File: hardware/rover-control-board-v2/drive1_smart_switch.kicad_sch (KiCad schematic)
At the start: 23 parts

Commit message: progress
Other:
- moved on the sheet: C2, C3
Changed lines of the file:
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@@
 	)
 	(junction
-		(at 193.04 149.86)
+		(at 198.12 149.86)
 		(diameter 0)
 		(color 0 0 0 0)
@@
 	)
 	(junction
-		(at 193.04 129.54)
-		(diameter 0)
-		(color 0 0 0 0)
-	)
-	(junction
 		(at 177.8 121.92)
 		(diameter 0)
@@
 	)
 	(junction
-		(at 204.47 129.54)
+		(at 60.96 29.21)
 		(diameter 0)
 		(color 0 0 0 0)
 	)
 	(junction
-		(at 60.96 29.21)
+		(at 204.47 129.54)
 		(diameter 0)
 		(color 0 0 0 0)
@@
 	)
 	(junction
+		(at 198.12 129.54)
+		(diameter 0)
+		(color 0 0 0 0)
+	)
+	(junction
 		(at 215.9 121.92)
 		(diameter 0)
@@
 	(wire
 		(pts
-			(xy 204.47 135.89) (xy 204.47 129.54)
+			(xy 209.55 135.89) (xy 209.55 134.62)
 		)
 		(stroke
@@
 	(wire
 		(pts
-			(xy 193.04 143.51) (xy 193.04 149.86)
+			(xy 198.12 143.51) (xy 198.12 149.86)
 		)
 		(stroke
@@
 	(wire
 		(pts
-			(xy 193.04 135.89) (xy 193.04 129.54)
+			(xy 198.12 135.89) (xy 198.12 129.54)
 		)
 		(stroke
@@
 	(wire
 		(pts
-			(xy 193.04 149.86) (xy 204.47 149.86)
+			(xy 198.12 149.86) (xy 209.55 149.86)
 		)
 		(stroke
@@
 	(wire
 		(pts
-			(xy 204.47 149.86) (xy 204.47 143.51)
+			(xy 209.55 149.86) (xy 209.55 143.51)
 		)
 		(stroke
@@
 	(wire
 		(pts
-			(xy 193.04 129.54) (xy 204.47 129.54)
+			(xy 193.04 129.54) (xy 198.12 129.54)
 		)
 		(stroke
@@
 	(wire
 		(pts
-			(xy 193.04 151.13) (xy 193.04 149.86)
+			(xy 198.12 151.13) (xy 198.12 149.86)
+		)
+		(stroke
+			(width 0)
+			(type default)
+		)
+	)
+	(wire
+		(pts
+			(xy 204.47 129.54) (xy 204.47 134.62)
 		)
 		(stroke
@@
 	(wire
 		(pts
+			(xy 198.12 129.54) (xy 204.47 129.54)
+		)
+		(stroke
+			(width 0)
+			(type default)
+		)
+	)
+	(wire
+		(pts
 			(xy 63.5 30.48) (xy 63.5 29.21)
 		)
@@
 		(pts
 			(xy 31.75 57.15) (xy 31.75 58.42)
+		)
+		(stroke
+			(width 0)
+			(type default)
+		)
+	)
+	(wire
+		(pts
+			(xy 209.55 134.62) (xy 204.47 134.62)
 		)
 		(stroke
@@
 	(hierarchical_label "PWR_IN"
 		(shape input)
-		(at 204.47 129.54 0)
+		(at 204.47 132.08 0)
 		(effects
 			(font
@@
 	(symbol
 		(lib_id "power:GND")
-		(at 193.04 151.13 0)
+		(at 198.12 151.13 0)
 		(unit 1)
 		(body_style 1)
@@
 		(fields_autoplaced yes)
 		(property "Reference" "#PWR08"
-			(at 193.04 157.48 0)
+			(at 198.12 157.48 0)
 			(hide yes)
 			(show_name no)
@@
 		)
 		(property "Value" "GND"
-			(at 193.04 156.21 0)
+			(at 198.12 156.21 0)
 			(show_name no)
 			(do_not_autoplace no)
@@
 		)
 		(property "Footprint" ""
-			(at 193.04 151.13 0)
+			(at 198.12 151.13 0)
 			(hide yes)
 			(show_name no)
@@
 		)
 		(property "Datasheet" ""
-			(at 193.04 151.13 0)
+			(at 198.12 151.13 0)
 			(hide yes)
 			(show_name no)
@@
 		)
 		(property "Description" "Power symbol creates a global label with name \"GND\" , ground"
-			(at 193.04 151.13 0)
+			(at 198.12 151.13 0)
 			(hide yes)
 			(show_name no)
@@
 	(symbol
 		(lib_id "Device:C")
-		(at 193.04 139.7 0)
+		(at 198.12 139.7 0)
 		(unit 1)
 		(body_style 1)
@@
 		(dnp no)
 		(property "Reference" "C2"
-			(at 195.58 138.43 0)
+			(at 200.66 138.43 0)
 			(show_name no)
 			(do_not_autoplace no)
@@
 		)
 		(property "Value" "10nF"
-			(at 195.58 140.97 0)
+			(at 200.66 140.97 0)
 			(show_name no)
 			(do_not_autoplace no)
@@
 		)
 		(property "Footprint" ""
-			(at 194.0052 143.51 0)
+			(at 199.0852 143.51 0)
 			(hide yes)
 			(show_name no)
@@
 		)
 		(property "Datasheet" ""
-			(at 193.04 139.7 0)
+			(at 198.12 139.7 0)
 			(hide yes)
 			(show_name no)
@@
 		)
 		(property "Description" "Unpolarized capacitor"
-			(at 193.04 139.7 0)
+			(at 198.12 139.7 0)
 			(hide yes)
 			(show_name no)
@@
 	(symbol
 		(lib_id "Device:C")
-		(at 204.47 139.7 0)
+		(at 209.55 139.7 0)
 		(unit 1)
 		(body_style 1)
@@
 		(dnp no)
 		(property "Reference" "C3"
-			(at 207.01 138.43 0)
+			(at 212.09 138.43 0)
 			(show_name no)
 			(do_not_autoplace no)
@@
 		)
 		(property "Value" "100nF"
-			(at 207.01 140.97 0)
+			(at 212.09 140.97 0)
 			(show_name no)
 			(do_not_autoplace no)
@@
 		)
 		(property "Footprint" ""
-			(at 205.4352 143.51 0)
+			(at 210.5152 143.51 0)
 			(hide yes)
 			(show_name no)
@@
 		)
 		(property "Datasheet" ""
-			(at 204.47 139.7 0)
+			(at 209.55 139.7 0)
 			(hide yes)
 			(show_name no)
@@
 		)
 		(property "Description" "Unpolarized capacitor"
-			(at 204.47 139.7 0)
-			(hide yes)
-			(show_name no)
+			(at 209.55 139.7 0)
+			(hide yes)
+			(show_name no)

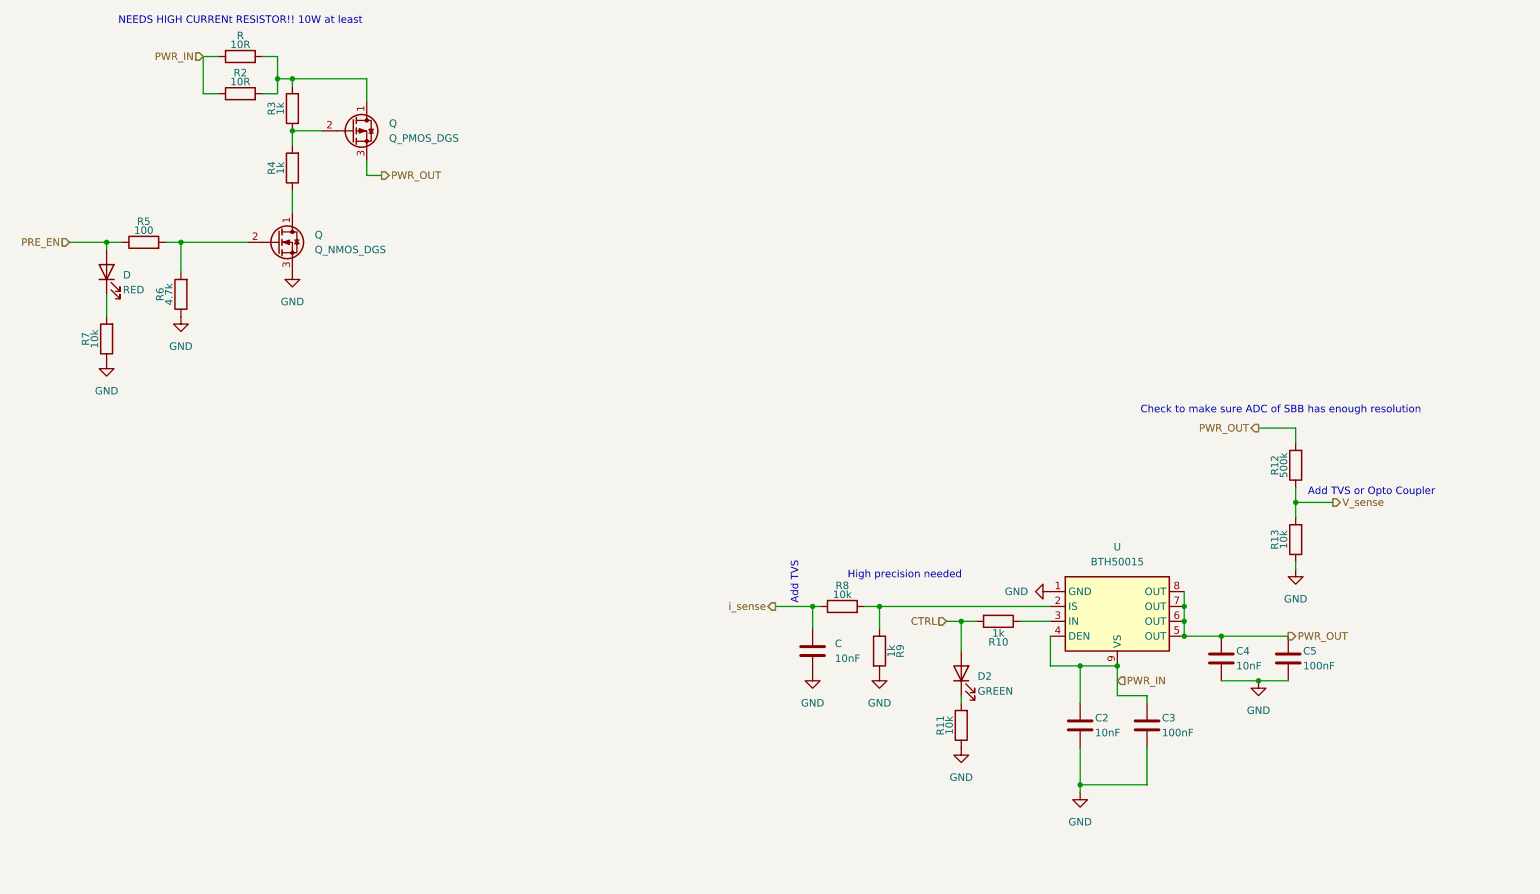
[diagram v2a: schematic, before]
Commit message: Channels routed, temp bus pending
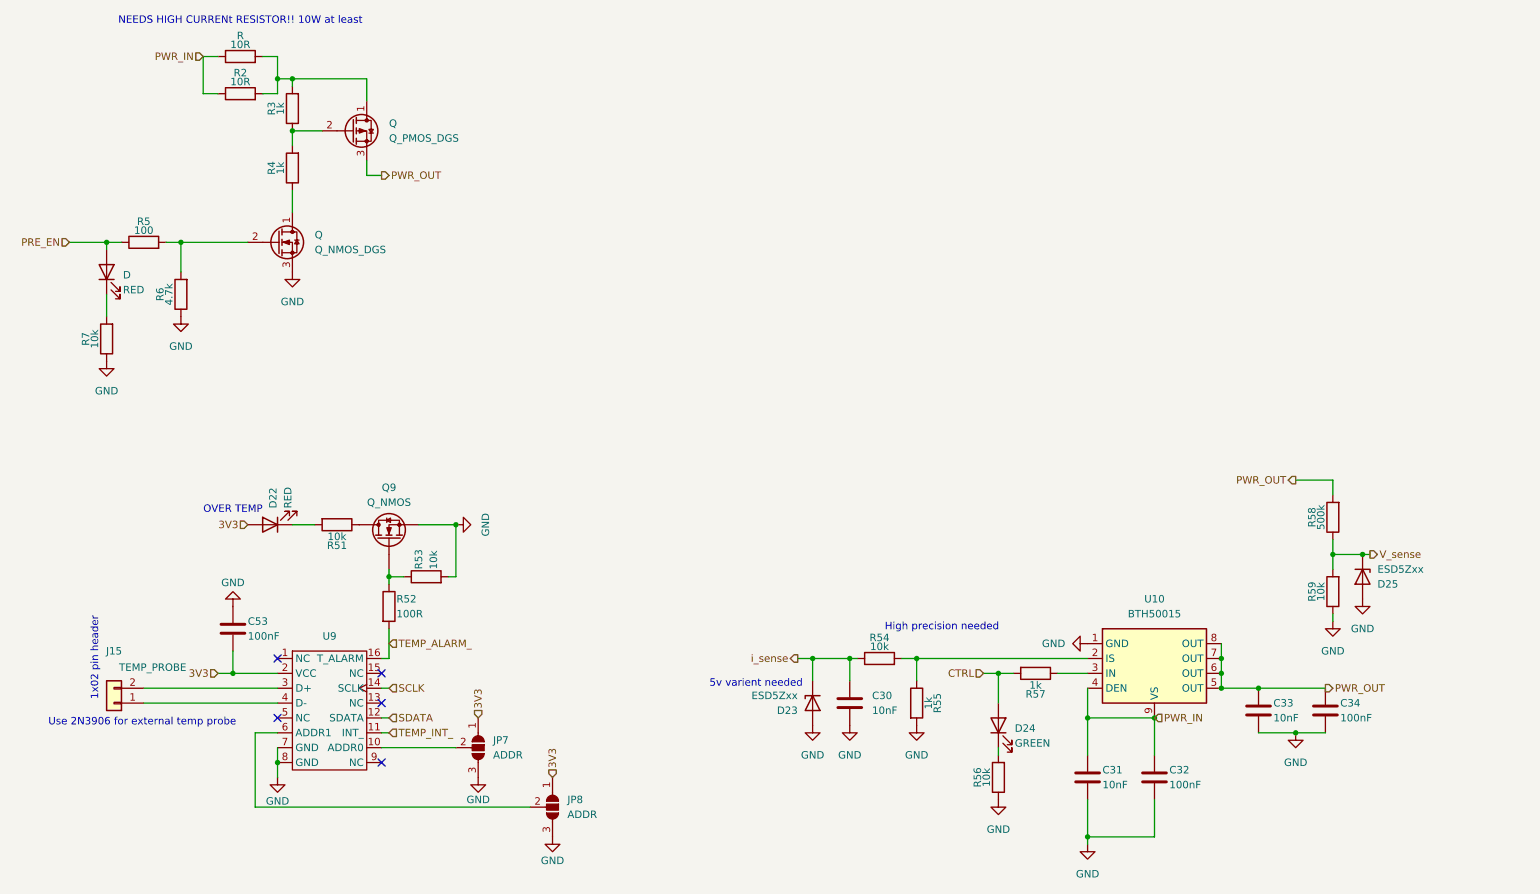
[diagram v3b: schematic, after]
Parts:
- removed C, C2, C4: 10nF, symbol Device:C
- removed C3, C5: 100nF, symbol Device:C
- removed D2: GREEN, symbol Device:LED
- removed R10, R9: 1k, symbol Device:R
- removed R11, R13, R8: 10k, symbol Device:R
- removed R12: 500k, symbol Device:R
- removed U: BTH50015, Package_SO:Infineon_PG-TSDSO-14-22, symbol component_library:BTH50015
- added C30, C31, C33: 10nF, symbol Device:C
- added C32, C34, C53: 100nF, symbol Device:C
- added D22: RED, symbol Device:LED
- added D23, D25: ESD5Zxx, Diode_SMD:D_SOD-523, symbol Diode:ESD5Zxx
- added D24: GREEN, symbol Device:LED
- added J15: TEMP_PROBE, symbol Connector_Generic:Conn_01x02
- added JP7, JP8: ADDR, Jumper:SolderJumper-3_P1.3mm_Open_Pad1.0x1.5mm, symbol Jumper:SolderJumper_3_Open
- added Q9: Q_NMOS, symbol Device:Q_NMOS
- added R51, R53, R54, R56, R59: 10k, symbol Device:R
- added R52: 100R, symbol Device:R
- added R55, R57: 1k, symbol Device:R
- added R58: 500k, symbol Device:R
- added U10: BTH50015, Package_SO:Infineon_PG-TSDSO-14-22, symbol component_library:BTH50015
- added U9: (no value), footprints:LM82, symbol component_library:LM82
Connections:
- net CTRL: now also D24.2 (A), R57.2
- net GND: now also C30.2, C31.2, C32.2, C33.2, C34.2, C53.1, D23.2 (A), D25.2 (A), JP7.3 (B), JP8.3 (B), Q9.S, R53.2, R55.2, R56.1, R59.1, U10.1 (GND), U9.7 (GND), U9.8 (GND)
- net PWR_IN: now also C31.1, C32.1, U10.4 (DEN), U10.9 (VS)
- net PWR_OUT: now also C33.1, C34.1, R58.2, U10.5 (OUT), U10.6 (OUT), U10.7 (OUT), U10.8 (OUT)
- net V_sense: now also D25.1 (K), R58.1, R59.2
- net i_sense: now also C30.1, D23.1 (K), R54.1
- new net: JP8.2 (C), U9.6 (ADDR1)
- new net: R54.2, R55.1, U10.2 (IS)
- new net: Q9.G, R52.1, R53.1
- new net: D24.1 (K), R56.2
- new net: Q9.D, R51.1
- new net: D22.1 (K), R51.2
- new net: R57.1, U10.3 (IN)
- new net: JP7.2 (C), U9.10 (ADDR0)
- new net: J15.2 (Pin_2), U9.3 (D+)
- new net: J15.1 (Pin_1), U9.4 (D-)
- new net 3V3: C53.2, D22.2 (A), JP7.1 (A), JP8.1 (A), U9.2 (VCC)
- new net SCLK: U9.14 (SCLK)
- new net SDATA: U9.12 (SDATA)
- new net TEMP_ALARM_: R52.2, U9.16 (T_ALARM)
- new net TEMP_INT_: U9.11 (INT_)
- no-connect marks 0 -> 5
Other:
- note added: "1x02 pin header"
- note added: "5v varient needed"
- note added: "OVER TEMP"
- note added: "Use 2N3906 for external temp probe"
- note removed: "Add TVS"
- note removed: "Add TVS or Opto Coupler"
- note removed: "Check to make sure ADC of SBB has enough resolution"

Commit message: Bus routed
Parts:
- renumbered C53 to C34, C30 to C35, C31 to C36, C32 to C37, C33 to C38, C34 to C39, D to D20, D22 to D21, D23 to D22, D24 to D23, D25 to D24, J15 to J13, Q to Q12, Q to Q13, Q9 to Q14, R7 to R62, R5 to R63, R6 to R64, R to R65, R2 to R66, R3 to R67, R4 to R68, R51 to R69, R52 to R70, R53 to R71, R54 to R72, R55 to R73, R56 to R74, R57 to R75, R58 to R76, R59 to R77, U9 to U11, U10 to U12

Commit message: revamping channel switches
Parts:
- renumbered C34 to C28, C35 to C29, C36 to C30, C37 to C31, C38 to C32, C39 to C33, J13 to J14, R62 to R61, R63 to R62, R64 to R63, R65 to R64, R66 to R65, R67 to R66, R68 to R67, R69 to R68, R70 to R69, R71 to R70, R72 to R71, R73 to R72, R74 to R73, R75 to R74, R76 to R75, R77 to R76, U11 to U10, U12 to U11

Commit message: Minor fixes and sanity checks
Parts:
- removed C29, C32: 10nF, symbol Device:C
- removed D22, D24: ESD5Zxx, Diode_SMD:D_SOD-523, symbol Diode:ESD5Zxx
- removed D23: GREEN, symbol Device:LED
- removed R71, R73, R76: 10k, symbol Device:R
- removed R72, R74: 1k, symbol Device:R
- removed R75: 500k, symbol Device:R
- removed U11: BTH50015, Package_SO:Infineon_PG-TSDSO-14-22, symbol component_library:BTH50015
- added C32: C_Polarized, Capacitor_SMD:CP_Elec_10x10.5, symbol Device:C_Polarized
- added D20: GREEN, symbol Device:LED
- added D21: ESD5Zxx, Diode_SMD:D_SOD-523, symbol Diode:ESD5Zxx
- added F4: Blade, symbol Device:Fuse
- added Q18: CSD19533Q5A, Package_TO_SOT_SMD:TDSON-8-1, symbol Transistor_FET:CSD19533Q5A
- added R67, R69: 10k, symbol Device:R
- added R68: 500k, symbol Device:R
- added U14: LTC7001, Package_SO:MSOP-10-1EP_3x3mm_P0.5mm_EP1.68x1.88mm, symbol component_library:LTC7001
- added U15: ACS37003, Package_SO:SOIC-16W_7.5x10.3mm_P1.27mm, symbol component_library:ACS37003
- C30: value 10nF -> 100nF
- C31: value 100nF -> 0.1uF
- renumbered C28 to C29, D20 to D18, D21 to D19, J14 to J15, Q12 to Q15, Q13 to Q16, Q14 to Q17, R61 to R57, R62 to R58, R63 to R59, R64 to R60, R65 to R61, R66 to R62, R67 to R63, R68 to R64, R69 to R65, R70 to R66, U10 to U13
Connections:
- net 3V3: now also C33.2, U15.13 (VCC)
- net CTRL: now also D20.2 (A), U14.4 (INP)
- net GND: now also C30.1, C33.1, C32.2, D21.2 (A), R67.1, R69.1, U14.11 (PAD), U14.2 (VCCUV), U14.3 (GND), U14.5 (OVLO), U15.16 (GND); no longer C30.2, C31.2, C33.2
- net PWR_IN: now also C32.1, Q18.5 (D); no longer C30.1, C31.1
- net PWR_OUT: now also F4.1, R68.2; no longer C33.1
- net V_sense: now also D21.1 (K), R68.1, R69.2
- net TEMP_INT_: no longer names the net of U13.11 (INT_)
- new net: Q18.1 (S), Q18.2 (S), Q18.3 (S), U15.1 (IP+), U15.2 (IP+), U15.3 (IP+), U15.4 (IP+)
- new net: F4.2, U15.5 (IP-), U15.6 (IP-), U15.7 (IP-), U15.8 (IP-)
- new net: D20.1 (K), R67.2
- new net: Q18.4 (G), U14.6 (TGDN), U14.7 (TGUP)
- new net: C30.2, U14.1 (VCC)
- new net: C31.2, U14.8 (TS)
- new net: C31.1, U14.9 (BST)
- new net VIOUT: U15.12 (VIOUT)
- new net VI_VREF: U15.11 (VREF)
- no-connect marks 5 -> 11
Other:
- note removed: "5v varient needed"
- note removed: "High precision needed"
